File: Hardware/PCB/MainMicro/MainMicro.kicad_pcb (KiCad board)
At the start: 2 copper layers, 66.5 x 76.2 mm, 49 parts, among them J1 Conn_02x05_Odd_Even, J2 USB_B_Mini, J3 Barrel_Jack, J4 Conn_01x05_Male, J5 Conn_01x06_Male, J6 Conn_01x06_Male, Q1 BSS138, Q2 BSS138, Q3 BSS138, Q4 BSS138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

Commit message: Big PCB changes
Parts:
- removed Q1, Q2, Q3, Q4, Q5, Q6: BSS138, Package_TO_SOT_SMD:SOT-23
- removed R16: 10k, Resistor_SMD:R_0805_2012Metric_Pad1.20x1.40mm_HandSolder
- added C13: .1u, Capacitor_SMD:C_0805_2012Metric_Pad1.18x1.45mm_HandSolder, B.Cu at (167.6, 83.1)
- added C14: .1u, Capacitor_SMD:C_0805_2012Metric_Pad1.18x1.45mm_HandSolder, B.Cu at (165.1, 82.0)
- added C15: .1u, Capacitor_SMD:C_0805_2012Metric_Pad1.18x1.45mm_HandSolder, B.Cu at (161.5, 83.1)
- added H1: MountingHole, MountingHole:MountingHole_2.7mm_M2.5, F.Cu at (210.3, 117.9)
- added H2: MountingHole, MountingHole:MountingHole_2.7mm_M2.5, F.Cu at (210.3, 69.8)
- added H3: MountingHole, MountingHole:MountingHole_2.7mm_M2.5, F.Cu at (151.9, 117.9)
- added H4: MountingHole, MountingHole:MountingHole_2.7mm_M2.5, F.Cu at (151.6, 69.6)
- added J10: Conn_01x03_Male, Connector_JST:JST_EH_B3B-EH-A_1x03_P2.50mm_Vertical, F.Cu at (193.1, 69.3)
- added J11: Conn_01x05_Male, Connector_JST:JST_EH_B5B-EH-A_1x05_P2.50mm_Vertical, F.Cu at (204.3, 87.4)
- added J12: Conn_01x05_Male, Connector_JST:JST_EH_B5B-EH-A_1x05_P2.50mm_Vertical, F.Cu at (210.6, 87.4)
- added J7: Conn_01x03_Male, Connector_JST:JST_EH_B3B-EH-A_1x03_P2.50mm_Vertical, F.Cu at (163.1, 118.6)
- added J8: Conn_01x03_Male, Connector_JST:JST_EH_B3B-EH-A_1x03_P2.50mm_Vertical, F.Cu at (210.1, 81.3)
- added J9: Conn_01x03_Male, Connector_JST:JST_EH_B3B-EH-A_1x03_P2.50mm_Vertical, F.Cu at (204.0, 75.2)
- added U5: SN74AVC8T245PW, Package_SO:TSSOP-24_4.4x7.8mm_P0.65mm, F.Cu at (166.6, 82.5)
- C1, C2, C3, FB1, R2: moved to B.Cu
- J3: footprint Connector_BarrelJack:BarrelJack_SwitchcraftConxall_RAPC10U_Horizontal -> Connector_BarrelJack:BarrelJack_CUI_PJ-102AH_Horizontal
- R10: value 10k -> 10
- R11, R12, R13, R14, R15, R5, R6, R7, R8, R9: value 10k -> 10; moved to B.Cu
- moved J1 159.3 mm to (190.8, 117.3), turned to 90 degrees
- moved R15 126.8 mm to (206.0, 101.6)
- moved C2 117.2 mm to (178.1, 103.1), turned to 180 degrees
- moved C1 116.2 mm to (171.4, 105.7), turned to 90 degrees
- moved R14 115.8 mm to (200.2, 93.2), turned to 90 degrees
- moved J6 113.0 mm to (158.0, 69.3)
- moved R8 109.2 mm to (190.8, 108.7), turned to -90 degrees
- moved R9 108.2 mm to (195.8, 109.0), turned to -90 degrees
- moved FB1 107.6 mm to (189.2, 97.3)
- moved R12 107.0 mm to (198.9, 73.9)
- moved U1 106.8 mm to (177.0, 107.4)
- moved R5 105.5 mm to (184.1, 74.5), turned to -90 degrees
- moved C3 104.4 mm to (172.5, 78.5), turned to 90 degrees
- moved D1 104.2 mm to (179.3, 112.3)
- moved R1 104.0 mm to (175.3, 112.3), turned to 180 degrees
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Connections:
- D2 pad 2: +5V -> Net-(D2-Pad2)
- J1 pad 2: /SWDIO_IN -> Net-(J1-Pad2)
- J1 pad 5: /SWIM -> unconnected-(J1-Pad5)
- J1 pad 6: /SWCLK_IN -> Net-(J1-Pad6)
- J3 pad 1: +5V -> Net-(D2-Pad2)
- J4 pad 2: /SPI1_MOSI -> Net-(J4-Pad2)
- J4 pad 3: /SPI1_MISO -> Net-(J4-Pad3)
- J4 pad 4: /SPI1_SCK -> Net-(J4-Pad4)
- R10 pad 1: +3V3 -> /Limit_SW1
- R10 pad 2: /PB8_GPO -> Net-(J7-Pad1)
- R11 pad 1: +5V -> /Limit_SW2
- R11 pad 2: /PUL1+ -> Net-(J8-Pad1)
- R12 pad 1: +5V -> /Limit_SW3
- R12 pad 2: /DIR1+ -> Net-(J9-Pad1)
- R13 pad 1: +5V -> /Limit_SW4
- R13 pad 2: /EN1+ -> Net-(J10-Pad1)
- R14 pad 1: +5V -> /IR_Sensor_IO1
- R14 pad 2: /PUL2+ -> Net-(J11-Pad3)
- R15 pad 1: +5V -> /IR_Sensor_IO2
- R15 pad 2: /DIR2+ -> Net-(J12-Pad3)
- R5 pad 1: +3V3 -> Net-(J4-Pad4)
- R5 pad 2: /PA8_GPO -> /SPI1_SCK
- R6 pad 1: +3V3 -> Net-(J4-Pad2)
- R6 pad 2: /PA9_GPO -> /SPI1_MOSI
- R7 pad 1: +3V3 -> Net-(J4-Pad3)
- R7 pad 2: /PB7_GPO -> /SPI1_MISO
- R8 pad 1: +3V3 -> /SWDIO_IN
- R8 pad 2: /PA10_GPO -> Net-(J1-Pad2)
- R9 pad 1: +3V3 -> /SWCLK_IN
- R9 pad 2: /PA11_GPO -> Net-(J1-Pad6)
- U2 pad 40: unconnected-(U2-Pad40) -> /Limit_SW1
- U2 pad 51: unconnected-(U2-Pad51) -> /Limit_SW2
- U2 pad 52: unconnected-(U2-Pad52) -> /Limit_SW3
- U2 pad 53: unconnected-(U2-Pad53) -> /Limit_SW4
- U2 pad 58: unconnected-(U2-Pad58) -> /PB6_GPO
- U2 pad 62: unconnected-(U2-Pad62) -> /PB9_GPO
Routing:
- net +5V: track 0.00 -> 189.6 mm, vias 0 -> 8
- net /NRST: track 0.00 -> 51.0 mm, vias 0 -> 5
- net /PA8_GPO: track 0.00 -> 44.7 mm, vias 0 -> 2
- net /PA9_GPO: track 0.00 -> 42.6 mm, vias 0 -> 2
- net /PA10_GPO: track 0.00 -> 41.3 mm, vias 0 -> 2
- net /PA11_GPO: track 0.00 -> 39.1 mm
- net GND: track 36.5 -> 72.1 mm, vias 11 -> 20
- net /PB9_GPO: track 0.00 -> 31.2 mm
- net /Limit_SW1: track 0.00 -> 28.7 mm, vias 0 -> 2
- net /SWCLK_IN: track 0.00 -> 24.8 mm, vias 0 -> 1
- net /PB8_GPO: track 0.00 -> 23.8 mm, vias 0 -> 2
- net /PB7_GPO: track 0.00 -> 23.2 mm, vias 0 -> 2
- net /EN2+: track 0.00 -> 23.0 mm
- net +3V3: track 48.5 -> 71.0 mm, vias 10 -> 12
- net /PB6_GPO: track 0.00 -> 21.9 mm
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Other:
- board size 66.5 x 76.2 mm -> 65.8 x 81.3 mm

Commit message: PCB passing DRC
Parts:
- added R16: 10, Resistor_SMD:R_0805_2012Metric_Pad1.20x1.40mm_HandSolder, B.Cu at (155.2, 85.3)
- added R17: 10, Resistor_SMD:R_0805_2012Metric_Pad1.20x1.40mm_HandSolder, B.Cu at (155.2, 83.1)
- added R18: 10, Resistor_SMD:R_0805_2012Metric_Pad1.20x1.40mm_HandSolder, B.Cu at (154.2, 78.2)
- added R19: 10, Resistor_SMD:R_0805_2012Metric_Pad1.20x1.40mm_HandSolder, B.Cu at (159.3, 73.4)
- added R20: 10, Resistor_SMD:R_0805_2012Metric_Pad1.20x1.40mm_HandSolder, B.Cu at (163.1, 73.7)
- added R21: 10, Resistor_SMD:R_0805_2012Metric_Pad1.20x1.40mm_HandSolder, B.Cu at (168.1, 73.7)
- J2: footprint Connector_USB:USB_Micro-AB_Molex_47590-0001 -> Connector_USB:USB_Micro-B_Amphenol_10118194_Horizontal
- moved J1 4.75 mm to (194.6, 114.5)
- moved J2 1.65 mm to (150.1, 97.3)
- moved C11 1.37 mm to (173.5, 92.7)
- moved C15 1.37 mm to (160.3, 82.5)
- moved C3 1.37 mm to (171.2, 78.0)
- moved C9 1.37 mm to (183.7, 98.0)
- moved H4 1.37 mm to (150.4, 69.1)
- moved J10 1.37 mm to (191.8, 68.8)
- moved J11 1.37 mm to (203.0, 86.9)
- moved J12 1.37 mm to (209.3, 86.9)
- moved R4 1.37 mm to (157.2, 89.9)
- moved SW1 1.37 mm to (178.3, 76.5)
- moved U4 1.37 mm to (176.8, 93.5)
- moved C10 1.37 mm to (166.1, 96.8)
- moved C12 1.37 mm to (173.5, 96.8)
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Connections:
- U5 pad 16: /EN2+ -> Net-(U5-Pad16)
- U5 pad 17: /DIR2+ -> Net-(U5-Pad17)
- U5 pad 18: /PUL2+ -> Net-(U5-Pad18)
- U5 pad 19: /EN1+ -> Net-(U5-Pad19)
- U5 pad 20: /DIR1+ -> Net-(U5-Pad20)
- U5 pad 21: /PUL1+ -> Net-(U5-Pad21)
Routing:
- net +3V3: track 71.0 -> 136.7 mm, vias 12 -> 16
- net /EN2+: track 23.0 -> 4.85 mm
- net /PUL2+: track 18.3 -> 3.59 mm
- net /DIR2+: track 19.2 -> 4.89 mm
- net Net-(U5-Pad16): track 0.00 -> 13.3 mm, vias 0 -> 1
- net /EN1+: track 18.1 -> 4.83 mm
- net unconnected-(J2-Pad6): track 0.00 -> 11.5 mm
- net Net-(U5-Pad17): track 0.00 -> 11.0 mm, vias 0 -> 1
- net Net-(U5-Pad19): track 0.00 -> 9.61 mm, vias 0 -> 1
- net Net-(U5-Pad18): track 0.00 -> 9.55 mm, vias 0 -> 1
- net /PUL1+: track 13.1 -> 4.10 mm
- net /DIR1+: track 13.5 -> 5.19 mm
- net Net-(U5-Pad21): track 0.00 -> 6.99 mm, vias 0 -> 1
- net Net-(U5-Pad20): track 0.00 -> 6.31 mm, vias 0 -> 1
- net /USB_D+: track 11.5 -> 13.4 mm, vias 0 -> 2
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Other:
- board size 65.8 x 81.3 mm -> 64.8 x 54.6 mm

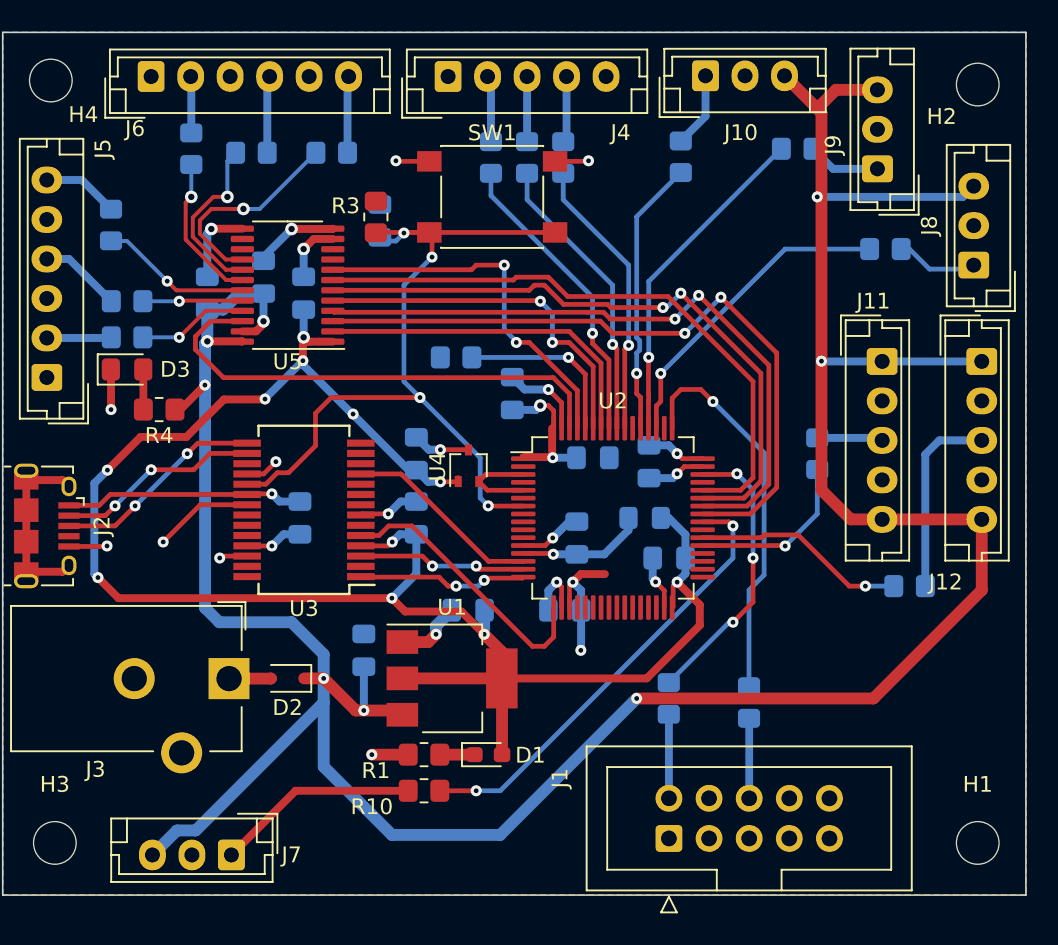
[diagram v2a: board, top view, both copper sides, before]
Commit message: Fixed Joe concerns
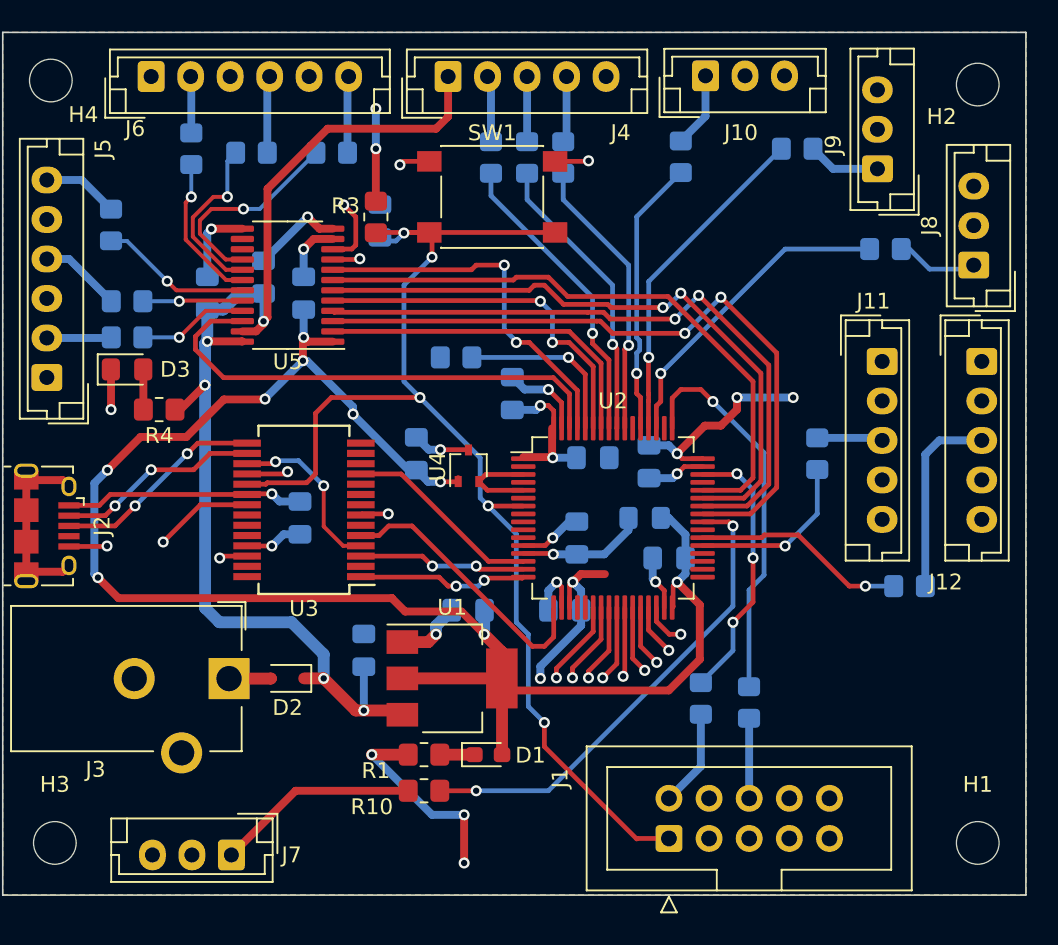
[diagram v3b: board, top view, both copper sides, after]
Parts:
- removed C12: .1u, Capacitor_SMD:C_0805_2012Metric_Pad1.18x1.45mm_HandSolder
- moved R8 2.03 mm to (191.5, 108.2)
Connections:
- J1 pad 1: /RST -> /NRST
- J1 pad 7: +3V3 -> unconnected-(J1-Pad7)
- J10 pad 3: +5V -> +3V3
- J11 pad 1: +5V -> +3V3
- J11 pad 5: +5V -> +3V3
- J12 pad 1: +5V -> +3V3
- J12 pad 5: +5V -> +3V3
- J4 pad 1: +3V3 -> +5V
- J7 pad 3: +5V -> +3V3
- J8 pad 3: +5V -> +3V3
- J9 pad 3: +5V -> +3V3
- U2 pad 22: unconnected-(U2-Pad22) -> /PA6
- U2 pad 23: unconnected-(U2-Pad23) -> /PA7
- U2 pad 24: unconnected-(U2-Pad24) -> /PC4
- U2 pad 25: unconnected-(U2-Pad25) -> /PC5
- U2 pad 26: unconnected-(U2-Pad26) -> /PB0
- U2 pad 27: unconnected-(U2-Pad27) -> /PB1
- U2 pad 28: unconnected-(U2-Pad28) -> /PB2
- U2 pad 29: unconnected-(U2-Pad29) -> /PB10
- U2 pad 30: unconnected-(U2-Pad30) -> /PB11
- U3 pad 17: unconnected-(U3-Pad17) -> Net-(U3-Pad17)
- U3 pad 4: +3V3 -> Net-(U3-Pad17)
- U5 pad 10: unconnected-(U5-Pad10) -> GND
- U5 pad 9: unconnected-(U5-Pad9) -> GND
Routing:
- net +5V: track 188.9 -> 75.7 mm, vias 8 -> 5
- net /NRST: track 51.8 -> 79.9 mm, vias 4 -> 5
- net GND: track 72.1 -> 87.4 mm, vias 20 -> 24
- net +3V3: track 136.7 -> 148.4 mm, vias 16 -> 18
- net Net-(U3-Pad17): track 0.00 -> 11.0 mm, vias 0 -> 2
- net /PA6: track 0.00 -> 5.41 mm, vias 0 -> 1
- net /PA7: track 0.00 -> 5.20 mm, vias 0 -> 1
- net /PC4: track 0.00 -> 4.98 mm, vias 0 -> 1
- net /PC5: track 0.00 -> 4.82 mm, vias 0 -> 1
- net /PB0: track 0.00 -> 4.40 mm, vias 0 -> 1
- net /PB1: track 0.00 -> 4.29 mm, vias 0 -> 1
- net /PB2: track 0.00 -> 3.89 mm, vias 0 -> 1
- net /PB10: track 0.00 -> 3.24 mm, vias 0 -> 1
- net /PB11: track 0.00 -> 2.76 mm, vias 0 -> 1
- net /Limit_SW1: track 28.7 -> 30.5 mm
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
